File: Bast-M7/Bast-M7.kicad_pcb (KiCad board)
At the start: 2 copper layers, 50.8 x 22.9 mm, 10 parts, among them J1 Conn_Battery, J3 Conn_Left, J4 Conn_Right, U1 W25Q128JVS, U2 MIMXRT1011DAE5A, U3 AP2112K-3.3

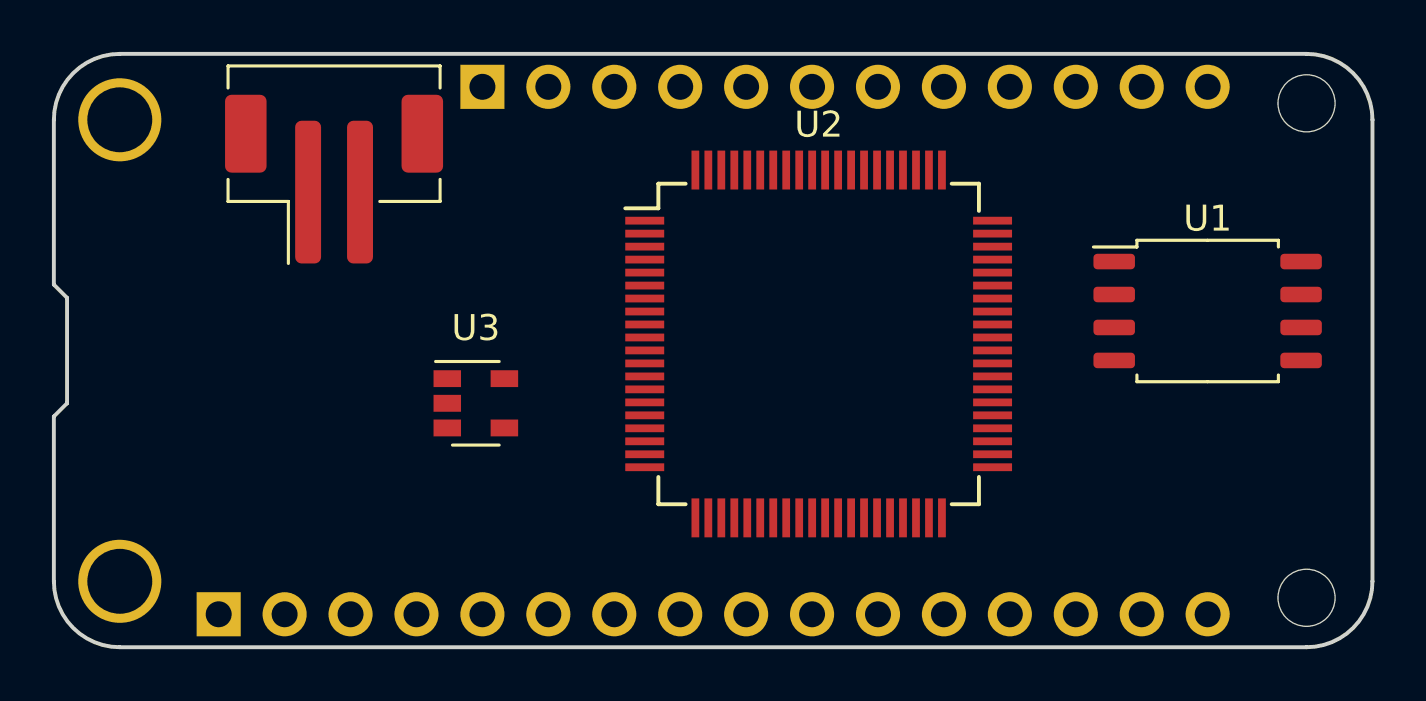
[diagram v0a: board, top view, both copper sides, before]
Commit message: Charger battery, fix Serial, and Boot pins
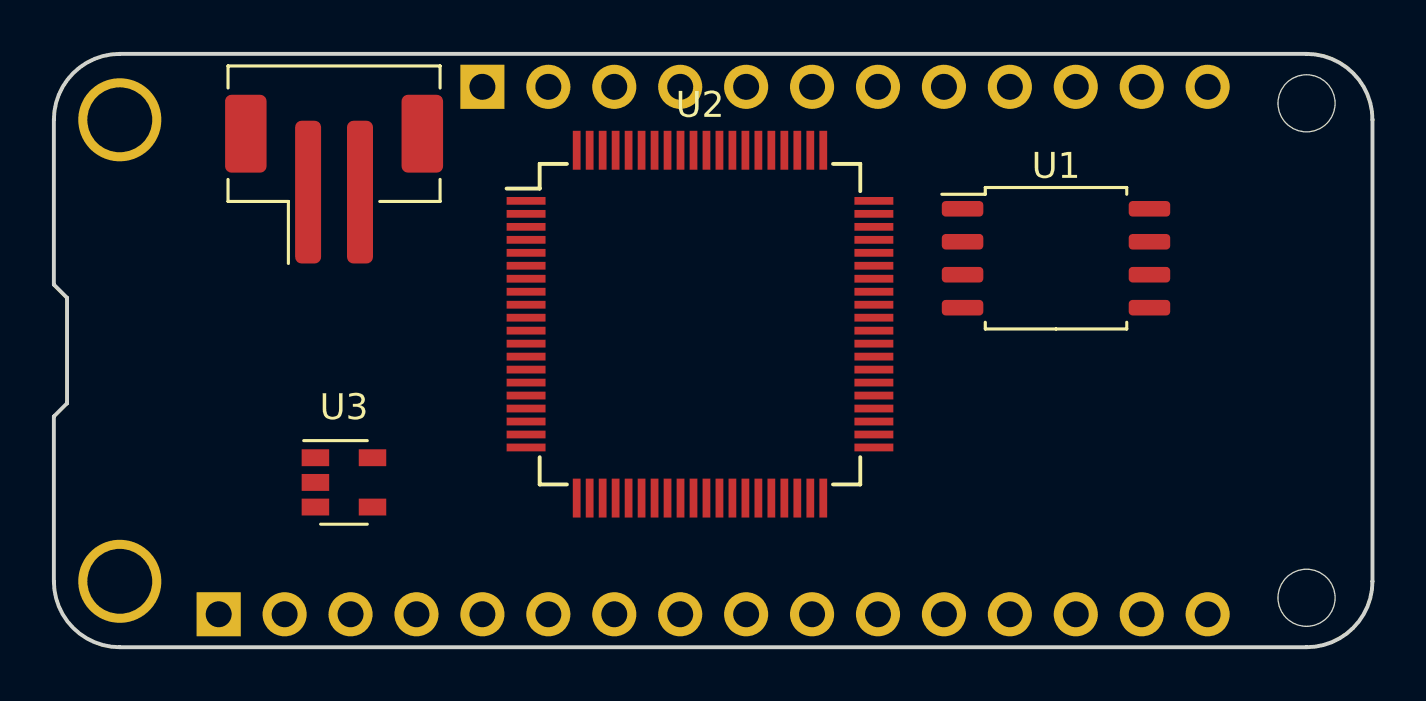
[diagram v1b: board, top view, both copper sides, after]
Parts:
- moved U1 6.19 mm to (165.6, 89.2)
- moved U3 5.92 mm to (138.2, 97.8)
- moved U2 4.64 mm to (151.9, 91.7)
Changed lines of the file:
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@@
   )
   (module Package_TO_SOT_SMD:SOT-23-5 (layer F.Cu)
-    (at 143.256 94.742)
+    (at 138.176 97.79)
     (descr "5-pin SOT23 package")
     (tags SOT-23-5)
@@
   )
   (module Package_QFP:TQFP-80_12x12mm_P0.5mm (layer F.Cu)
-    (at 156.464 92.456)
+    (at 151.892 91.694)
     (descr "80-Lead Plastic Thin Quad Flatpack (PT) - 12x12x1 mm Body, 2.00 mm [TQFP] (see Microchip Packaging Specification 00000049BS.pdf)")
     (tags "QFP 0.5")
@@
   )
   (module Package_SO:SOIC-8_5.23x5.23mm_P1.27mm (layer F.Cu)
-    (at 171.45 91.186)
+    (at 165.608 89.154)
     (descr "SOIC, 8 Pin (http://www.winbond.com/resource-files/w25q32jv%20revg%2003272018%20plus.pdf#page=68), generated with kicad-footprint-generator ipc_gullwing_generator.py")
     (tags "SOIC SO")
